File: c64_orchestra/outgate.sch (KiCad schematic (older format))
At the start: 0 parts

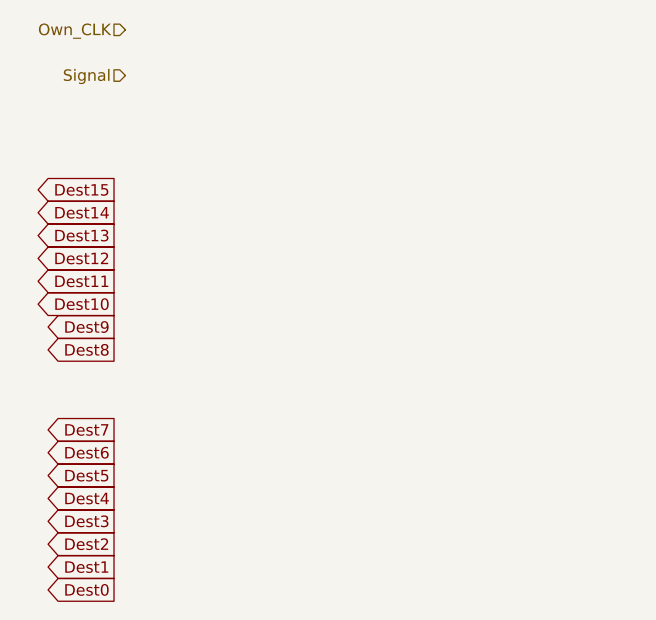
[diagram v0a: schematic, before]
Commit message: Added parts of schematic and worked on pcb layout.
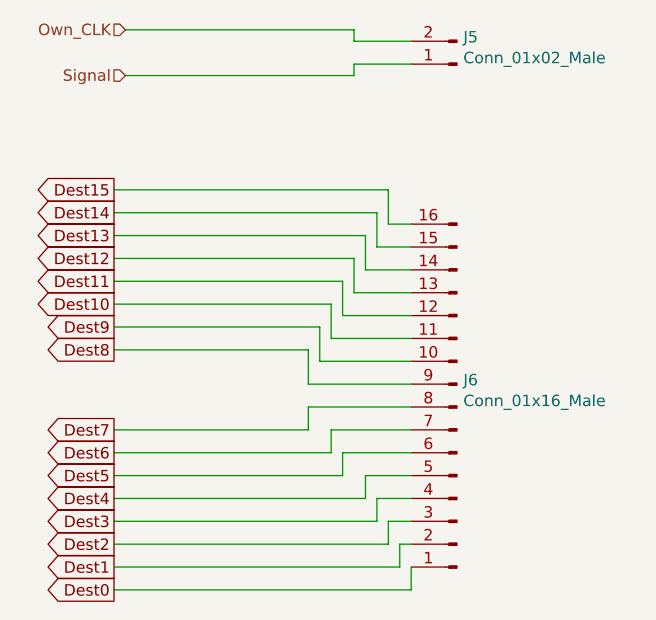
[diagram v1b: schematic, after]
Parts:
- added J5: Conn_01x02_Male, Connector_PinSocket_2.54mm:PinSocket_1x02_P2.54mm_Vertical, symbol Connector:Conn_01x02_Male
- added J6: Conn_01x16_Male, Connector_PinSocket_2.54mm:PinSocket_1x16_P2.54mm_Vertical, symbol Connector:Conn_01x16_Male
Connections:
- net Dest0: now also J6.1 (Pin_1)
- net Dest1: now also J6.2 (Pin_2)
- net Dest10: now also J6.11 (Pin_11)
- net Dest11: now also J6.12 (Pin_12)
- net Dest12: now also J6.13 (Pin_13)
- net Dest13: now also J6.14 (Pin_14)
- net Dest14: now also J6.15 (Pin_15)
- net Dest15: now also J6.16 (Pin_16)
- net Dest2: now also J6.3 (Pin_3)
- net Dest3: now also J6.4 (Pin_4)
- net Dest4: now also J6.5 (Pin_5)
- net Dest5: now also J6.6 (Pin_6)
- net Dest6: now also J6.7 (Pin_7)
- net Dest7: now also J6.8 (Pin_8)
- net Dest8: now also J6.9 (Pin_9)
- net Dest9: now also J6.10 (Pin_10)
- net Own_CLK: now also J5.2 (Pin_2)
- net Signal: now also J5.1 (Pin_1)
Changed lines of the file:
@@
 Text GLabel 1550 2900 0    50   Output ~ 0
 Dest15
+$Comp
+L Connector:Conn_01x16_Male J6
+U 1 1 5FB3FA8C
+P 3050 3850
+F 0 "J6" H 3022 3732 50  0000 R CNN
+F 1 "Conn_01x16_Male" H 3022 3823 50  0000 R CNN
+F 2 "Connector_PinSocket_2.54mm:PinSocket_1x16_P2.54mm_Vertical" H 3050 3850 50  0001 C CNN
+F 3 "~" H 3050 3850 50  0001 C CNN
+	1    3050 3850
+	-1   0    0    1
+$EndComp
+$Comp
+L Connector:Conn_01x02_Male J5
+U 1 1 5FB416E0
+P 3050 2350
+F 0 "J5" H 3022 2232 50  0000 R CNN
+F 1 "Conn_01x02_Male" H 3022 2323 50  0000 R CNN
+F 2 "Connector_PinSocket_2.54mm:PinSocket_1x02_P2.54mm_Vertical" H 3050 2350 50  0001 C CNN
+F 3 "~" H 3050 2350 50  0001 C CNN
+	1    3050 2350
+	-1   0    0    1
+$EndComp
+Wire Wire Line
+	1600 2200 2600 2200
+Wire Wire Line
+	2600 2200 2600 2250
+Wire Wire Line
+	2600 2250 2850 2250
+Wire Wire Line
+	1600 2400 2600 2400
+Wire Wire Line
+	2600 2400 2600 2350
+Wire Wire Line
+	2600 2350 2850 2350
+Wire Wire Line
+	1550 4650 2850 4650
+Wire Wire Line
+	2850 4650 2850 4550
+Wire Wire Line
+	1550 4550 2800 4550
+Wire Wire Line
+	2800 4550 2800 4450
+Wire Wire Line
+	2800 4450 2850 4450
+Wire Wire Line
+	1550 4450 2750 4450
+Wire Wire Line
+	2750 4450 2750 4350
+Wire Wire Line
+	2750 4350 2850 4350
+Wire Wire Line
+	1550 4350 2700 4350
+Wire Wire Line
+	2700 4350 2700 4250
+Wire Wire Line
+	2700 4250 2850 4250
+Wire Wire Line
+	1550 4250 2650 4250
+Wire Wire Line
+	2650 4250 2650 4150
+Wire Wire Line
+	2650 4150 2850 4150
+Wire Wire Line
+	2850 4050 2550 4050
+Wire Wire Line
+	2550 4050 2550 4150
+Wire Wire Line
+	2550 4150 1550 4150
+Wire Wire Line
+	1550 4050 2500 4050
+Wire Wire Line
+	2500 4050 2500 3950
+Wire Wire Line
+	2500 3950 2850 3950
+Wire Wire Line
+	2850 3850 2400 3850
+Wire Wire Line
+	2400 3850 2400 3950
+Wire Wire Line
+	2400 3950 1550 3950
+Wire Wire Line
+	1550 3600 2400 3600
+Wire Wire Line
+	2400 3600 2400 3750
+Wire Wire Line
+	2400 3750 2850 3750
+Wire Wire Line
+	1550 3500 2450 3500
+Wire Wire Line
+	2450 3500 2450 3650
+Wire Wire Line
+	2450 3650 2850 3650
+Wire Wire Line
+	1550 3400 2500 3400
+Wire Wire Line
+	2500 3400 2500 3550
+Wire Wire Line
+	2500 3550 2850 3550
+Wire Wire Line
+	1550 3300 2550 3300
+Wire Wire Line
+	2550 3300 2550 3450
+Wire Wire Line
+	2550 3450 2850 3450
+Wire Wire Line
+	1550 3200 2600 3200
+Wire Wire Line
+	2600 3200 2600 3350
+Wire Wire Line
+	2600 3350 2850 3350
+Wire Wire Line
+	1550 3100 2650 3100
+Wire Wire Line
+	2650 3100 2650 3250
+Wire Wire Line
+	2650 3250 2850 3250
+Wire Wire Line
+	1550 3000 2700 3000
+Wire Wire Line
+	2700 3000 2700 3150
+Wire Wire Line
+	2700 3150 2850 3150
+Wire Wire Line
+	1550 2900 2750 2900
+Wire Wire Line
+	2750 2900 2750 3050
+Wire Wire Line
+	2750 3050 2850 3050
 $EndSCHEMATC
